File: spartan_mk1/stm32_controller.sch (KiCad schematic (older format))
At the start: 26 parts, among them SW1 SW_SPDT, U4 STM32F405RGTx, Y1 X322516MLB4SI

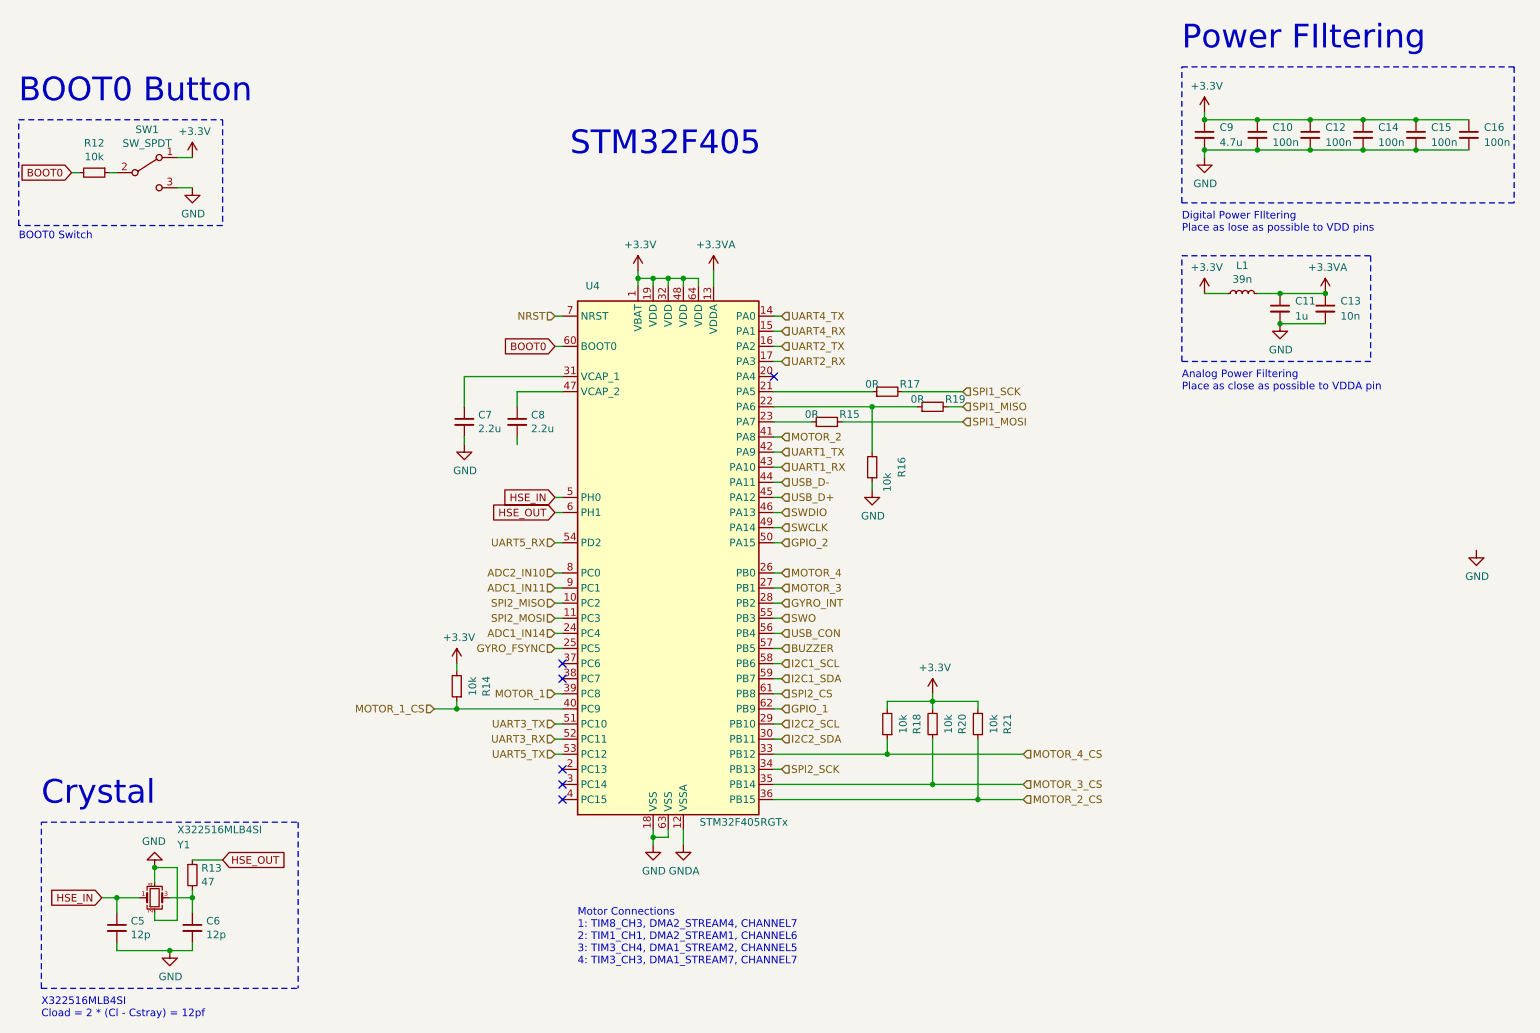
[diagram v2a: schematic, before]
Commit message: Almost complete PCB layout (no routing)
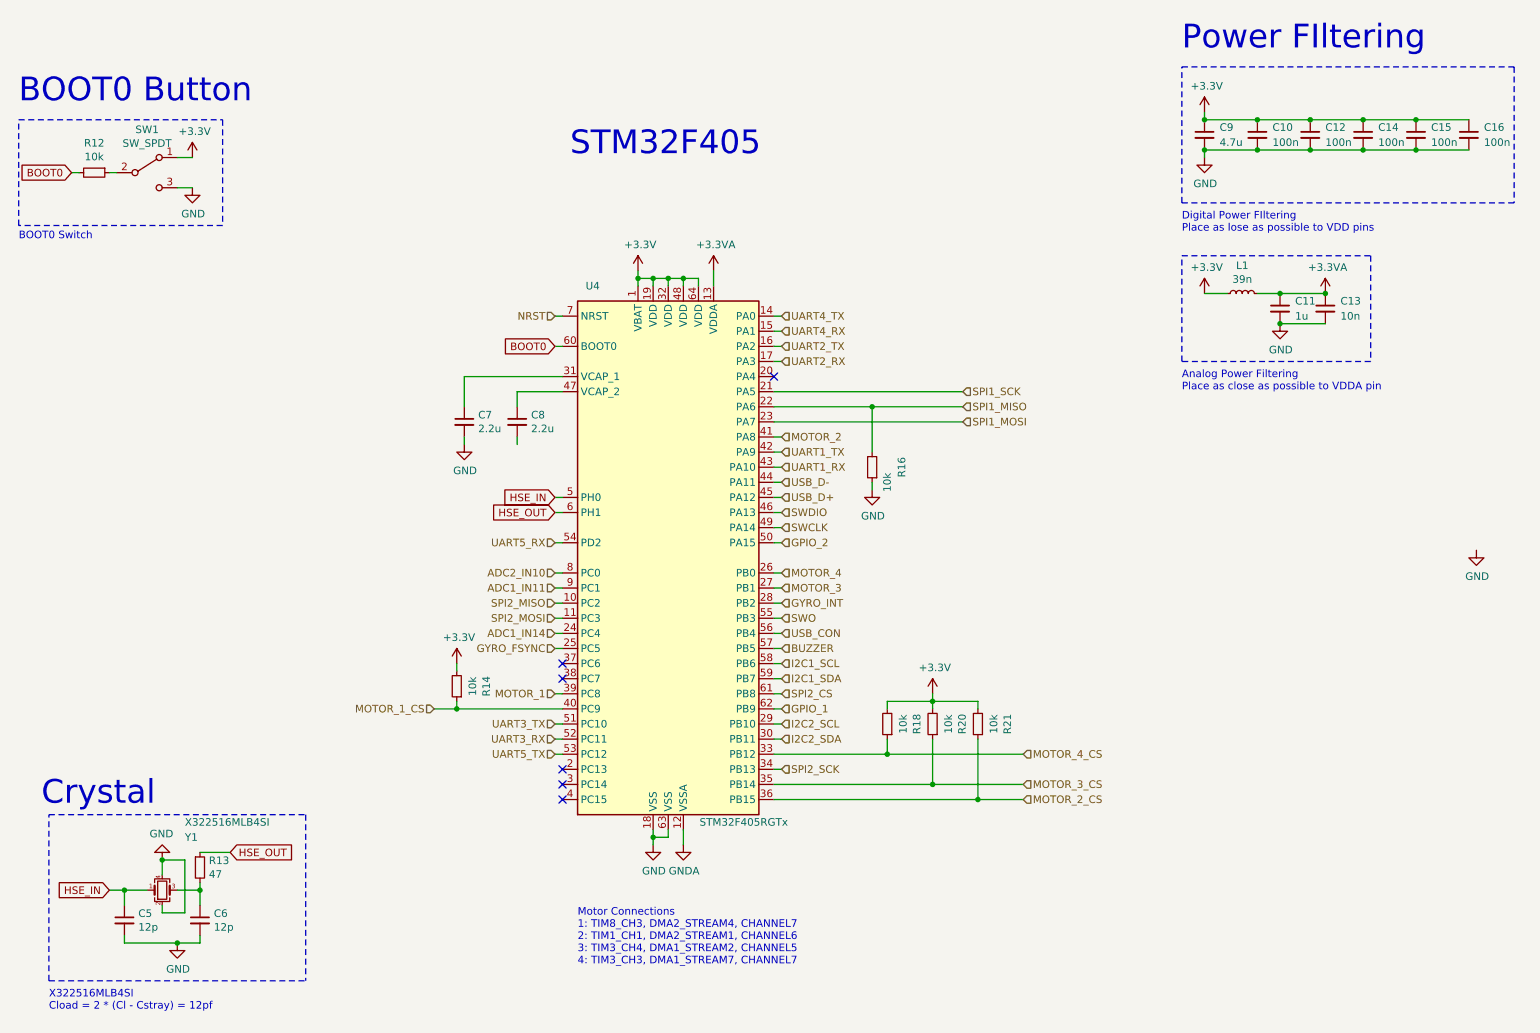
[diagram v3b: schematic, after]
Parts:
- removed R15, R17, R19: 0R, Resistor_SMD:R_0402_1005Metric, symbol Device:R_Small
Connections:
- net SPI1_MISO: now also R16.2, U4.22 (PA6)
- net SPI1_MOSI: now also U4.23 (PA7)
- net SPI1_SCK: now also U4.21 (PA5)
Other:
- moved on the sheet: C5, C6, R13, Y1
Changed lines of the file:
@@
 $EndDescr
 Wire Notes Line
-	1100 7150 1100 6050
-Text Notes 1100 7350 0    50   ~ 0
+	1150 7100 1150 6000
+Text Notes 1150 7300 0    50   ~ 0
 X322516MLB4SI\nCload = 2 * (Cl - Cstray) = 12pf
 $Comp
@@
 L Device:Crystal_GND24_Small Y1
 U 1 1 5F8717BB
-P 1850 6550
-F 0 "Y1" H 2000 6900 50  0000 L CNN
-F 1 "X322516MLB4SI" H 2000 7000 50  0000 L CNN
-F 2 "Crystal:Crystal_SMD_3225-4Pin_3.2x2.5mm" H 1850 6550 50  0001 C CNN
-F 3 "~" H 1850 6550 50  0001 C CNN
-	1    1850 6550
+P 1900 6500
+F 0 "Y1" H 2050 6850 50  0000 L CNN
+F 1 "X322516MLB4SI" H 2050 6950 50  0000 L CNN
+F 2 "Crystal:Crystal_SMD_3225-4Pin_3.2x2.5mm" H 1900 6500 50  0001 C CNN
+F 3 "~" H 1900 6500 50  0001 C CNN
+	1    1900 6500
 	1    0    0    -1
 $EndComp
@@
 L Device:C_Small C6
 U 1 1 5F873DD9
-P 2100 6750
-F 0 "C6" H 2192 6796 50  0000 L CNN
-F 1 "12p" H 2192 6705 50  0000 L CNN
-F 2 "Capacitor_SMD:C_0402_1005Metric" H 2100 6750 50  0001 C CNN
-F 3 "~" H 2100 6750 50  0001 C CNN
-	1    2100 6750
-	1    0    0    -1
-$EndComp
-Wire Wire Line
-	2100 6650 2100 6550
-Wire Wire Line
-	2100 6550 1950 6550
+P 2150 6700
+F 0 "C6" H 2242 6746 50  0000 L CNN
+F 1 "12p" H 2242 6655 50  0000 L CNN
+F 2 "Capacitor_SMD:C_0402_1005Metric" H 2150 6700 50  0001 C CNN
+F 3 "~" H 2150 6700 50  0001 C CNN
+	1    2150 6700
+	1    0    0    -1
+$EndComp
+Wire Wire Line
+	2150 6600 2150 6500
+Wire Wire Line
+	2150 6500 2000 6500
 $Comp
 L Device:C_Small C5
 U 1 1 5F8762DF
-P 1600 6750
-F 0 "C5" H 1692 6796 50  0000 L CNN
-F 1 "12p" H 1692 6705 50  0000 L CNN
-F 2 "Capacitor_SMD:C_0402_1005Metric" H 1600 6750 50  0001 C CNN
-F 3 "~" H 1600 6750 50  0001 C CNN
-	1    1600 6750
-	1    0    0    -1
-$EndComp
-Wire Wire Line
-	1600 6650 1600 6550
-Wire Wire Line
-	1600 6550 1750 6550
-Wire Wire Line
-	1850 6450 1850 6350
-Wire Wire Line
-	1850 6700 1850 6650
+P 1650 6700
+F 0 "C5" H 1742 6746 50  0000 L CNN
+F 1 "12p" H 1742 6655 50  0000 L CNN
+F 2 "Capacitor_SMD:C_0402_1005Metric" H 1650 6700 50  0001 C CNN
+F 3 "~" H 1650 6700 50  0001 C CNN
+	1    1650 6700
+	1    0    0    -1
+$EndComp
+Wire Wire Line
+	1650 6600 1650 6500
+Wire Wire Line
+	1650 6500 1800 6500
+Wire Wire Line
+	1900 6400 1900 6300
+Wire Wire Line
+	1900 6650 1900 6600
 $Comp
 L power:GND #PWR032
 U 1 1 5F878A49
-P 1950 6900
-F 0 "#PWR032" H 1950 6650 50  0001 C CNN
-F 1 "GND" H 1955 6727 50  0000 C CNN
-F 2 "" H 1950 6900 50  0001 C CNN
-F 3 "" H 1950 6900 50  0001 C CNN
-	1    1950 6900
-	1    0    0    -1
-$EndComp
-Wire Wire Line
-	2100 6850 2100 6900
-Wire Wire Line
-	2100 6900 1950 6900
-Wire Wire Line
-	1950 6900 1600 6900
-Wire Wire Line
-	1600 6900 1600 6850
-Connection ~ 1950 6900
-Wire Wire Line
-	2000 6700 2000 6350
-Wire Wire Line
-	1850 6350 2000 6350
-Wire Wire Line
-	1850 6700 2000 6700
+P 2000 6850
+F 0 "#PWR032" H 2000 6600 50  0001 C CNN
+F 1 "GND" H 2005 6677 50  0000 C CNN
+F 2 "" H 2000 6850 50  0001 C CNN
+F 3 "" H 2000 6850 50  0001 C CNN
+	1    2000 6850
+	1    0    0    -1
+$EndComp
+Wire Wire Line
+	2150 6800 2150 6850
+Wire Wire Line
+	2150 6850 2000 6850
+Wire Wire Line
+	2000 6850 1650 6850
+Wire Wire Line
+	1650 6850 1650 6800
+Connection ~ 2000 6850
+Wire Wire Line
+	2050 6650 2050 6300
+Wire Wire Line
+	1900 6300 2050 6300
+Wire Wire Line
+	1900 6650 2050 6650
 $Comp
 L power:GND #PWR031
 U 1 1 5F87D117
-P 1850 6350
-F 0 "#PWR031" H 1850 6100 50  0001 C CNN
-F 1 "GND" H 1855 6177 50  0000 C CNN
-F 2 "" H 1850 6350 50  0001 C CNN
-F 3 "" H 1850 6350 50  0001 C CNN
-	1    1850 6350
+P 1900 6300
+F 0 "#PWR031" H 1900 6050 50  0001 C CNN
+F 1 "GND" H 1905 6127 50  0000 C CNN
+F 2 "" H 1900 6300 50  0001 C CNN
+F 3 "" H 1900 6300 50  0001 C CNN
+	1    1900 6300
 	-1   0    0    1
 $EndComp
-Connection ~ 1850 6350
+Connection ~ 1900 6300
 $Comp
 L Device:R_Small R13
 U 1 1 5F87F7DC
-P 2100 6400
-F 0 "R13" H 2159 6446 50  0000 L CNN
-F 1 "47" H 2159 6355 50  0000 L CNN
-F 2 "Resistor_SMD:R_0603_1608Metric" H 2100 6400 50  0001 C CNN
-F 3 "~" H 2100 6400 50  0001 C CNN
-	1    2100 6400
-	1    0    0    -1
-$EndComp
-Wire Wire Line
-	2100 6500 2100 6550
-Connection ~ 2100 6550
-Wire Wire Line
-	2100 6300 2300 6300
-Text GLabel 2300 6300 2    50   Input ~ 0
+P 2150 6350
+F 0 "R13" H 2209 6396 50  0000 L CNN
+F 1 "47" H 2209 6305 50  0000 L CNN
+F 2 "Resistor_SMD:R_0603_1608Metric" H 2150 6350 50  0001 C CNN
+F 3 "~" H 2150 6350 50  0001 C CNN
+	1    2150 6350
+	1    0    0    -1
+$EndComp
+Wire Wire Line
+	2150 6450 2150 6500
+Connection ~ 2150 6500
+Wire Wire Line
+	2150 6250 2350 6250
+Text GLabel 2350 6250 2    50   Input ~ 0
 HSE_OUT
-Text GLabel 1500 6550 0    50   Input ~ 0
+Text GLabel 1550 6500 0    50   Input ~ 0
 HSE_IN
 Wire Wire Line
-	1500 6550 1600 6550
-Connection ~ 1600 6550
-Wire Notes Line
-	2800 6050 2800 7150
-Wire Notes Line
-	1100 6050 2800 6050
-Wire Notes Line
-	1100 7150 2800 7150
+	1550 6500 1650 6500
+Connection ~ 1650 6500
+Wire Notes Line
+	2850 6000 2850 7100
+Wire Notes Line
+	1150 6000 2850 6000
+Wire Notes Line
+	1150 7100 2850 7100
 Text HLabel 6000 3900 2    50   Input ~ 0
 USB_D+
@@
 	5950 3300 6600 3300
 Connection ~ 6600 3300
-$Comp
-L Device:R_Small R19
-U 1 1 5FA43726
-P 7000 3300
-F 0 "R19" V 7050 3150 50  0000 C CNN
-F 1 "0R" V 7050 3400 50  0000 C CNN
-F 2 "Resistor_SMD:R_0402_1005Metric" H 7000 3300 50  0001 C CNN
-F 3 "~" H 7000 3300 50  0001 C CNN
-	1    7000 3300
-	0    -1   -1   0
-$EndComp
-$Comp
-L Device:R_Small R17
-U 1 1 5FA43DD8
-P 6700 3200
-F 0 "R17" V 6750 3050 50  0000 C CNN
-F 1 "0R" V 6750 3300 50  0000 C CNN
-F 2 "Resistor_SMD:R_0402_1005Metric" H 6700 3200 50  0001 C CNN
-F 3 "~" H 6700 3200 50  0001 C CNN
-	1    6700 3200
-	0    -1   -1   0
-$EndComp
-Wire Wire Line
-	7100 3300 7200 3300
-Wire Wire Line
-	6600 3300 6900 3300
-Wire Wire Line
-	7200 3200 6800 3200
-Wire Wire Line
-	5950 3200 6600 3200
-$Comp
-L Device:R_Small R15
-U 1 1 5FA5B03A
-P 6300 3400
-F 0 "R15" V 6350 3250 50  0000 C CNN
-F 1 "0R" V 6350 3500 50  0000 C CNN
-F 2 "Resistor_SMD:R_0402_1005Metric" H 6300 3400 50  0001 C CNN
-F 3 "~" H 6300 3400 50  0001 C CNN
-	1    6300 3400
-	0    -1   -1   0
-$EndComp
-Wire Wire Line
-	5950 3400 6200 3400
-Wire Wire Line
-	6400 3400 7200 3400
 Wire Wire Line
 	6600 3300 6600 3600
@@
 Wire Wire Line
 	5350 6100 5350 6200
+Wire Wire Line
+	5950 3200 7200 3200
+Wire Wire Line
+	5950 3400 7200 3400
+Wire Wire Line
+	6600 3300 7200 3300
 $EndSCHEMATC

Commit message: updated placement
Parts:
- removed SW1: SW_SPDT, symbol Switch:SW_SPDT
- added SW1: SW_SPST, switches_SMD_omron:SW_B3U-3000P, symbol Switch:SW_SPST
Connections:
- net +3V3: now also R12.1
- net BOOT0: now also SW1.1 (A)
- net GND: now also C8.2, SW1.2 (B)
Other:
- moved on the sheet: R12
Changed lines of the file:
@@
-	1    0    0    -1
-$EndComp
-$Comp
-L power:GND #PWR037
-U 1 1 5F82F59F
-P 10600 4250
-F 0 "#PWR037" H 10600 4000 50  0001 C CNN
-F 1 "GND" H 10605 4077 50  0000 C CNN
-F 2 "" H 10600 4250 50  0001 C CNN
-F 3 "" H 10600 4250 50  0001 C CNN
-	1    10600 4250
 	1    0    0    -1
 $EndComp
@@
 	3900 3550 3900 3500
 $Comp
-L Switch:SW_SPDT SW1
-U 1 1 5F830A70
-P 1800 1750
-F 0 "SW1" H 1800 2035 50  0000 C CNN
-F 1 "SW_SPDT" H 1800 1944 50  0000 C CNN
-F 2 "" H 1800 1750 50  0001 C CNN
-F 3 "~" H 1800 1750 50  0001 C CNN
-	1    1800 1750
-	1    0    0    -1
-$EndComp
-$Comp
 L Device:R_Small R12
 U 1 1 5F8314D8
-P 1450 1750
-F 0 "R12" V 1254 1750 50  0000 C CNN
-F 1 "10k" V 1345 1750 50  0000 C CNN
-F 2 "Resistor_SMD:R_0402_1005Metric" H 1450 1750 50  0001 C CNN
-F 3 "~" H 1450 1750 50  0001 C CNN
-	1    1450 1750
+P 1750 1750
+F 0 "R12" V 1554 1750 50  0000 C CNN
+F 1 "10k" V 1645 1750 50  0000 C CNN
+F 2 "Resistor_SMD:R_0402_1005Metric" H 1750 1750 50  0001 C CNN
+F 3 "~" H 1750 1750 50  0001 C CNN
+	1    1750 1750
 	0    1    1    0
 $EndComp
 Text GLabel 1300 1750 0    50   Input ~ 0
 BOOT0
-Wire Wire Line
-	1300 1750 1350 1750
-Wire Wire Line
-	1600 1750 1550 1750
 $Comp
 L power:+3.3V #PWR033
 U 1 1 5F8334C6
-P 2100 1650
-F 0 "#PWR033" H 2100 1500 50  0001 C CNN
-F 1 "+3.3V" H 2115 1823 50  0000 C CNN
-F 2 "" H 2100 1650 50  0001 C CNN
-F 3 "" H 2100 1650 50  0001 C CNN
-	1    2100 1650
-	1    0    0    -1
-$EndComp
-Wire Wire Line
-	2100 1650 2000 1650
-$Comp
-L power:GND #PWR034
-U 1 1 5F8343AD
-P 2100 1850
-F 0 "#PWR034" H 2100 1600 50  0001 C CNN
-F 1 "GND" H 2105 1677 50  0000 C CNN
-F 2 "" H 2100 1850 50  0001 C CNN
-F 3 "" H 2100 1850 50  0001 C CNN
-	1    2100 1850
-	1    0    0    -1
-$EndComp
-Wire Wire Line
-	2100 1850 2000 1850
-Wire Notes Line
-	2300 1400 2300 2100
-Wire Notes Line
-	2300 2100 950  2100
-Wire Notes Line
-	950  2100 950  1400
+P 2000 1750
+F 0 "#PWR033" H 2000 1600 50  0001 C CNN
+F 1 "+3.3V" H 2015 1923 50  0000 C CNN
+F 2 "" H 2000 1750 50  0001 C CNN
+F 3 "" H 2000 1750 50  0001 C CNN
+	1    2000 1750
+	1    0    0    -1
+$EndComp
 Wire Notes Line
 	950  1400 2300 1400
@@
 Wire Wire Line
 	4500 4000 4550 4000
-Text Notes 950  2200 0    50   ~ 0
+Text Notes 950  2600 0    50   ~ 0
 BOOT0 Switch
 Wire Wire Line
@@
 Wire Wire Line
 	6600 3300 7200 3300
+Wire Wire Line
+	1850 1750 2000 1750
+Wire Wire Line
+	1300 1750 1500 1750
+Wire Wire Line
+	1500 1750 1500 1800
+Connection ~ 1500 1750
+Wire Wire Line
+	1500 1750 1650 1750
+$Comp
+L Switch:SW_SPST SW1
+U 1 1 5FA08604
+P 1500 2000
+F 0 "SW1" V 1454 2098 50  0000 L CNN
+F 1 "SW_SPST" V 1545 2098 50  0000 L CNN
+F 2 "switches_SMD_omron:SW_B3U-3000P" H 1500 2000 50  0001 C CNN
+F 3 "~" H 1500 2000 50  0001 C CNN
+	1    1500 2000
+	0    1    1    0
+$EndComp
+$Comp
+L power:GND #PWR034
+U 1 1 5F8343AD
+P 1500 2250
+F 0 "#PWR034" H 1500 2000 50  0001 C CNN
+F 1 "GND" H 1505 2077 50  0000 C CNN
+F 2 "" H 1500 2250 50  0001 C CNN
+F 3 "" H 1500 2250 50  0001 C CNN
+	1    1500 2250
+	1    0    0    -1
+$EndComp
+Wire Wire Line
+	1500 2250 1500 2200
+Wire Notes Line
+	2300 2500 950  2500
+Wire Notes Line
+	950  1400 950  2500
+Wire Notes Line
+	2300 1400 2300 2500
+$Comp
+L power:GND #PWR0101
+U 1 1 5FA81178
+P 4250 3550
+F 0 "#PWR0101" H 4250 3300 50  0001 C CNN
+F 1 "GND" H 4255 3377 50  0000 C CNN
+F 2 "" H 4250 3550 50  0001 C CNN
+F 3 "" H 4250 3550 50  0001 C CNN
+	1    4250 3550
+	1    0    0    -1
+$EndComp
 $EndSCHEMATC

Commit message: Routing in progress
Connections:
- net GNDA is gone; now on net GND: U4.12 (VSSA)
- net SPI2_CS: no longer names the net of U4.61 (PB8)
- net SPI2_MISO: no longer names the net of U4.10 (PC2)
- net SPI2_MOSI: no longer names the net of U4.11 (PC3)
- net SPI2_SCK: no longer names the net of U4.34 (PB13)
- net USB_CON: no longer names the net of U4.56 (PB4)
- no-connect marks 6 -> 11
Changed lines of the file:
@@
 $Descr A4 11693 8268
 encoding utf-8
-Sheet 4 6
+Sheet 6 6
 Title ""
 Date ""
@@
 	5150 6150 5150 6200
 Connection ~ 5150 6150
-$Comp
-L power:GNDA #PWR040
-U 1 1 5F82EBD9
-P 5350 6200
-F 0 "#PWR040" H 5350 5950 50  0001 C CNN
-F 1 "GNDA" H 5355 6027 50  0000 C CNN
-F 2 "" H 5350 6200 50  0001 C CNN
-F 3 "" H 5350 6200 50  0001 C CNN
-	1    5350 6200
-	1    0    0    -1
-$EndComp
 Wire Wire Line
 	4250 3550 4250 3500
@@
 Text HLabel 7200 3400 2    50   Input ~ 0
 SPI1_MOSI
-Text HLabel 6000 5700 2    50   Input ~ 0
-SPI2_SCK
-Wire Wire Line
-	6000 5700 5950 5700
-Text HLabel 4500 4600 0    50   Input ~ 0
-SPI2_MISO
-Text HLabel 4500 4700 0    50   Input ~ 0
-SPI2_MOSI
-Wire Wire Line
-	4500 4700 4550 4700
-Wire Wire Line
-	4500 4600 4550 4600
 Text HLabel 6000 4400 2    50   Input ~ 0
 MOTOR_4
@@
 Wire Wire Line
 	6600 3300 6600 3600
-Text HLabel 6000 5200 2    50   Input ~ 0
-SPI2_CS
 Wire Wire Line
 	6000 5300 5950 5300
 Text HLabel 6000 5300 2    50   Input ~ 0
 GPIO_1
-Wire Wire Line
-	6000 5200 5950 5200
 Text HLabel 6000 4000 2    50   Input ~ 0
 SWDIO
@@
 NoConn ~ 4550 5000
 NoConn ~ 4550 5100
-Text HLabel 6000 4800 2    50   Input ~ 0
-USB_CON
-Wire Wire Line
-	6000 4800 5950 4800
 Text HLabel 4500 4200 0    50   Input ~ 0
 UART5_RX
@@
 Wire Wire Line
 	4550 4400 4500 4400
-Wire Wire Line
-	5350 6100 5350 6200
 Wire Wire Line
 	5950 3200 7200 3200
@@
 	1    0    0    -1
 $EndComp
+NoConn ~ 5950 4800
+Wire Wire Line
+	5350 6100 5350 6150
+Wire Wire Line
+	5350 6150 5250 6150
+Connection ~ 5250 6150
+NoConn ~ 5950 5200
+NoConn ~ 5950 5700
+NoConn ~ 4550 4700
+NoConn ~ 4550 4600
 $EndSCHEMATC

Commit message: Routing complete. Passed DRC
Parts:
- added C17: 100n, Capacitor_SMD:C_0402_1005Metric, symbol Device:C_Small
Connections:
- net GND: now also C17.1
- net NRST: now also C17.2
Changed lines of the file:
@@
 Text Notes 4600 1650 0    157  ~ 0
 STM32F405\n
-Text HLabel 4500 2700 0    50   Input ~ 0
+Text HLabel 4300 2700 0    50   Input ~ 0
 NRST
-Wire Wire Line
-	4500 2700 4550 2700
 NoConn ~ 4550 5000
 NoConn ~ 4550 5100
@@
 NoConn ~ 4550 4700
 NoConn ~ 4550 4600
+$Comp
+L Device:C_Small C17
+U 1 1 5FA45722
+P 4400 2500
+F 0 "C17" H 4492 2546 50  0000 L CNN
+F 1 "100n" H 4492 2455 50  0000 L CNN
+F 2 "Capacitor_SMD:C_0402_1005Metric" H 4400 2500 50  0001 C CNN
+F 3 "~" H 4400 2500 50  0001 C CNN
+	1    4400 2500
+	1    0    0    -1
+$EndComp
+$Comp
+L power:GND #PWR011
+U 1 1 5FA46166
+P 4400 2350
+F 0 "#PWR011" H 4400 2100 50  0001 C CNN
+F 1 "GND" H 4405 2177 50  0000 C CNN
+F 2 "" H 4400 2350 50  0001 C CNN
+F 3 "" H 4400 2350 50  0001 C CNN
+	1    4400 2350
+	-1   0    0    1
+$EndComp
+Wire Wire Line
+	4400 2350 4400 2400
+Wire Wire Line
+	4300 2700 4400 2700
+Wire Wire Line
+	4400 2600 4400 2700
+Connection ~ 4400 2700
+Wire Wire Line
+	4400 2700 4550 2700
 $EndSCHEMATC
